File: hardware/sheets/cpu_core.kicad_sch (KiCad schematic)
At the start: 43 parts, among them U1 V20, U10 74HCT32, U11 74HCT125, U12 74HC157, U13 74HCT04, U14 TCM809, U2 74HCT573, U3 74HCT573, U4 74HCT573, U5 74HCT245, U6 74HCT138, U7 74HCT00, U8 74HCT74, U9 74HC161

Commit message: Symbols+parts: IS62WV51216, TL16C550CPT, I2C RTC; 3.3V LVC/HC rebinds
New flat mini-xt: symbols (gensym.py), pins verified against
jlc_get_pinout + datasheet (PCF8563 caught a jlc_get_pinout numbering bug):
IS62WV51216 (512Kx16 SRAM, TSOP-44), TL16C550PT (TL16C550C UART, LQFP-48,
NO.PT numbering -- distinct from the old DIP-40 16550 symbol), PCF8563
(I2C RTC, SO-8).

parts.py: bind the three new parts (SRAM in stock at JLC; TL16C550CPT
sourced elsewhere like the V20, 0 JLC stock; PCF8563 + CR2032 holder on
Device:Battery_Cell); rebind the clock dividers to 74LVC74A/74LVC161
(check 7: HC/HCT both fail fmax margin at 3.3V/14.318MHz); add LVC-grade
binds for 5V-tolerant-input octal parts (74LVC573A/244A/574A/125A/245A)
and plain-HC binds for pure-3.3V-domain gates (74HC00/04/32/138) on the
existing HCT-body symbols; add 74LVC2G07 as a value override on the
pin-identical 74LVC2G06 body. Delete the now-dead AS6C4008 DIP-32 socket,
16550 PLCC-44 socket, and DS12C887 DIP-24 socket entries (replaced parts,
no longer sourced).

Sanity build (build.py) still passes: root + 13 sheets, exit 0. The three
deleted entries leave their still-unrewired sheets (cpu_core, com_port,
rtc) temporarily unmapped in check_parts.py until Tasks 4-9 rewire them --
expected transitional state, not a regression.

Co-Authored-By: Claude Fable 5 <noreply@anthropic.com>
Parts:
- RAM1, RAM2: footprint Package_DIP:DIP-32_W15.24mm_Socket -> (none); LCSC Part Num C2874017 -> (none)
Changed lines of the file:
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@@
 			)
 		)
-		(property "Footprint" "Package_DIP:DIP-32_W15.24mm_Socket"
-			(at 302.26 76.2 0)
-			(effects
-				(font
-					(size 1.27 1.27)
-				)
-				(hide yes)
-			)
-		)
-		(property "LCSC Part Num" "C2874017"
+		(property "Footprint" ""
 			(at 302.26 76.2 0)
 			(effects
@@
 			)
 		)
-		(property "Footprint" "Package_DIP:DIP-32_W15.24mm_Socket"
+		(property "Footprint" ""
 			(at 302.26 175.26 0)
 			(effects
-				(font
-					(size 1.27 1.27)
-				)
-				(hide yes)
-			)
-		)
-		(property "LCSC Part Num" "C2874017"
-			(at 302.26 175.26 0)
-			(effects

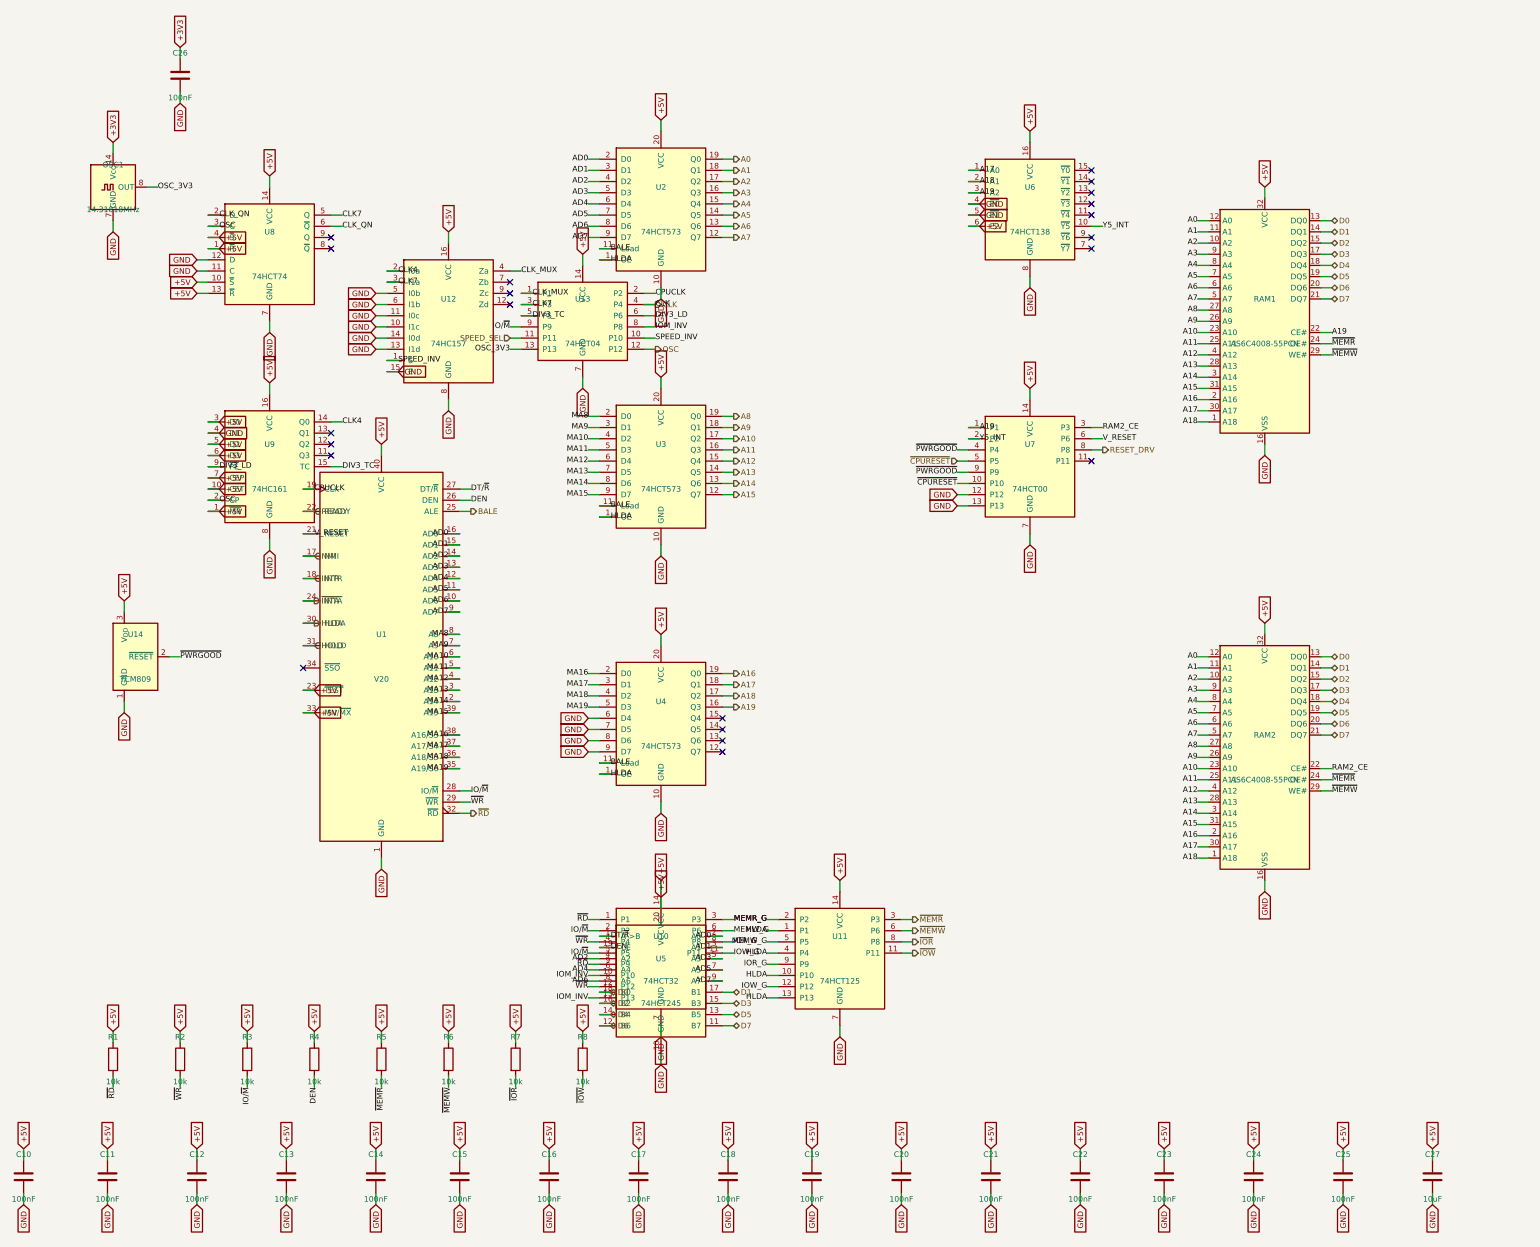
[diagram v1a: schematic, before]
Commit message: cpu_core: LVC573A/245A 3.3V boundary; single 512Kx16 SRAM as 1Mx8
Convert the CPU core to the 3.3V single-board design (spec 2026-07-14): the V20
and its demux latches/transceiver become the board's single 5V<->3.3V boundary.

- Address latches U2-U4 -> 74LVC573A, data xcvr U5 -> 74LVC245A, strobe tri-state
  U11 -> 74LVC125A, all @ +3V3 with 5V-tolerant CPU-side inputs (the boundary).
  U10 74HCT32 stays @ +5V (reads the raw 5V V20 strobes); U13 74HCT04 stays @ +5V
  (V20 CLK needs Vkh=4.0V, Task1 check 1).
- Glue U6 138 / U7 00 -> 74HC values @ +3V3; dividers U8/U9 -> 74LVC74A/74LVC161
  @ +3V3 (Task1 check 7 fmax). Speed mux U12 @ +3V3, select driven directly by
  the 3.3V SPEED_SEL (I0a/I1a un-swapped); U13's freed SPEED gate parked.
- Reset: V20 RESET driven directly from 3.3V logic (Task1 check 1, no buffer);
  TCM809 U14 -> +3V3.
- Memory: drop 2x AS6C4008 + the SRAM#2 select NAND; place 1x IS62WV51216BLL
  512Kx16 as 1Mx8 (byte-lane trick: A0->LB, A0_INV->UB, both IO bytes on D0-D7).
  /CE = NOT(Y5_INT) via a freed U7 NAND-as-inverter (answers 1MB less the
  0xA0000-0xBFFFF video window); A0_INV via the other freed U7 gate.
- Decoupling pool -> +3V3 (drop the removed SRAM's caps); explicit +5V caps for
  the surviving 5V parts.

Decisions logged in hardware/notes/questions-cpu_core.md.

Co-Authored-By: Claude Fable 5 <noreply@anthropic.com>
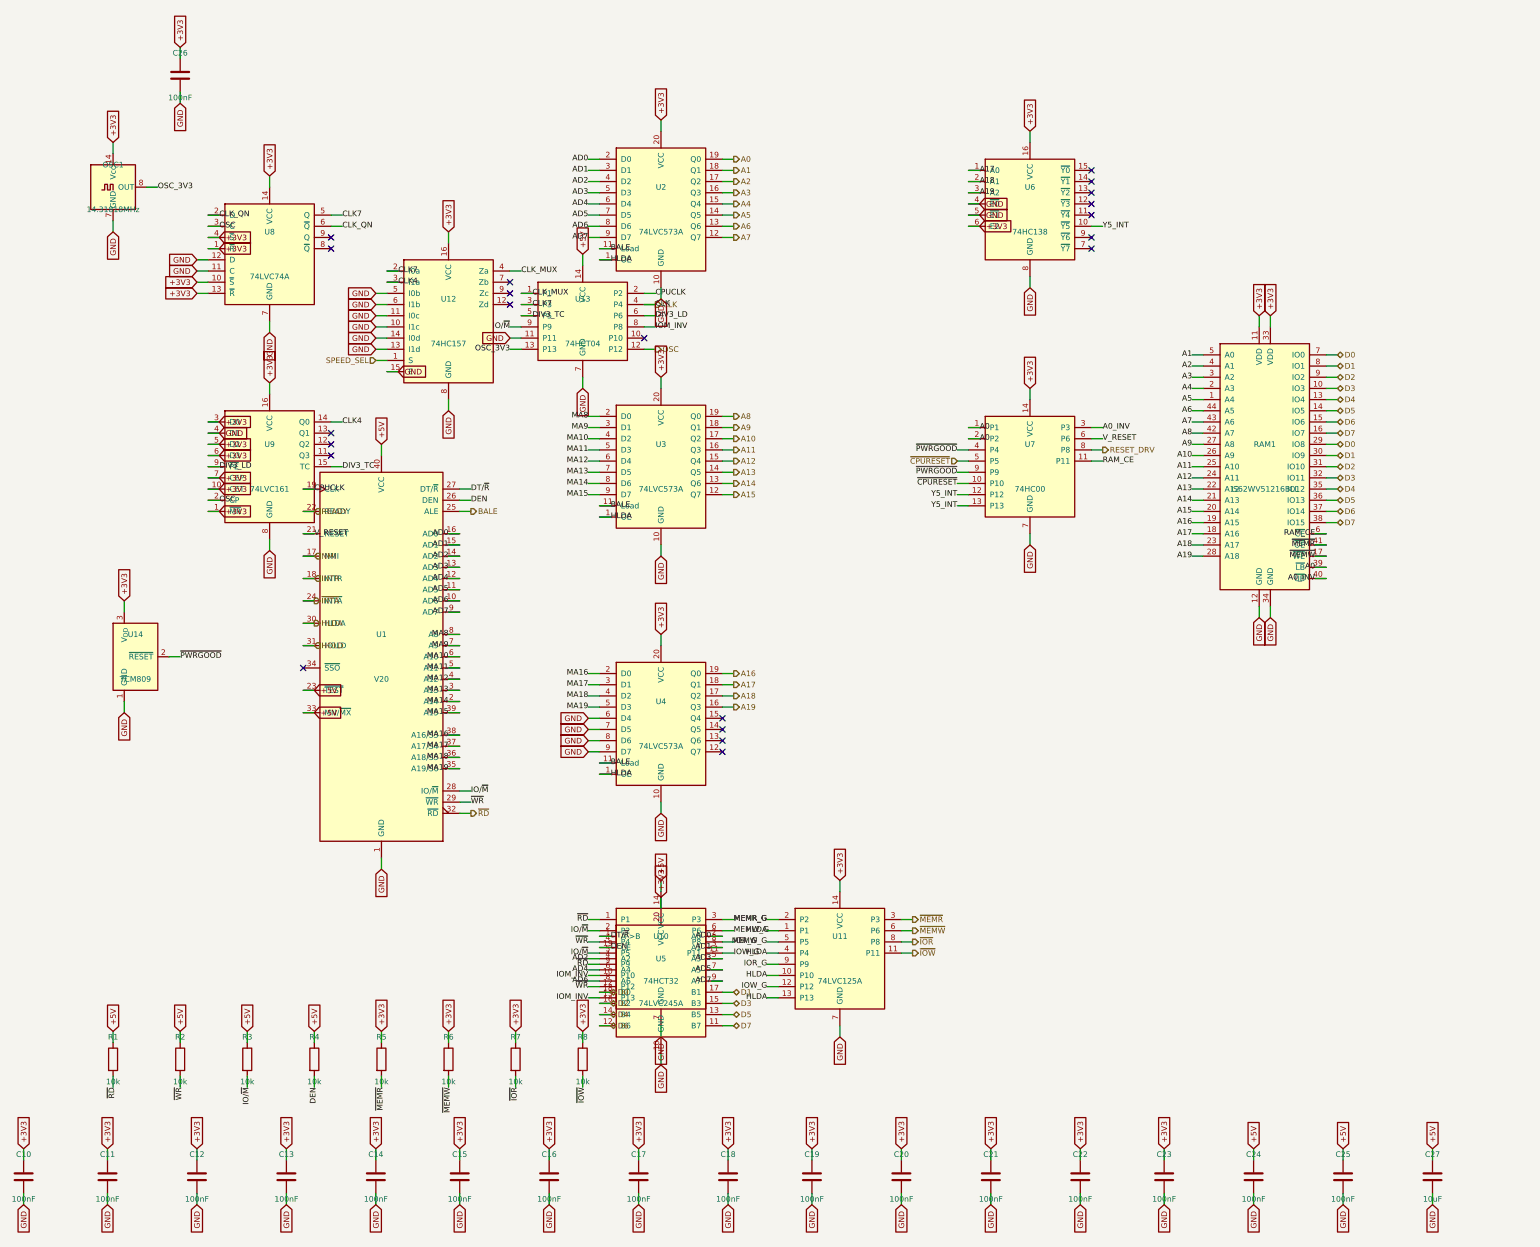
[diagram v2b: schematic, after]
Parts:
- removed RAM1, RAM2: AS6C4008-55PCN, symbol Memory_RAM:AS6C4008-55PCN
- added RAM1: IS62WV51216BLL, Package_SO:TSOP-II-44_10.16x18.41mm_P0.8mm, symbol mini-xt:IS62WV51216
- U11: value 74HCT125 -> 74LVC125A; LCSC Part Num C5962 -> C6057
- U2, U3, U4: value 74HCT573 -> 74LVC573A; footprint Package_SO:SOIC-20W_7.5x12.8mm_P1.27mm -> Package_SO:TSSOP-20_4.4x6.5mm_P0.65mm; LCSC Part Num C5209384 -> C6096
- U5: value 74HCT245 -> 74LVC245A; footprint Package_SO:SOIC-20W_7.5x12.8mm_P1.27mm -> Package_SO:TSSOP-20_4.4x6.5mm_P0.65mm; LCSC Part Num C5979 -> C6082
- U6: value 74HCT138 -> 74HC138; LCSC Part Num C5965 -> C5602
- U7: value 74HCT00 -> 74HC00; LCSC Part Num C282337 -> C699445
- U8: value 74HCT74 -> 74LVC74A; footprint Package_SO:SOIC-14_3.9x8.7mm_P1.27mm -> Package_SO:TSSOP-14_4.4x5mm_P0.65mm; LCSC Part Num C686657 -> C6100
- U9: value 74HC161 -> 74LVC161; footprint Package_SO:SOIC-16_3.9x9.9mm_P1.27mm -> Package_SO:TSSOP-16_4.4x5mm_P0.65mm; LCSC Part Num C5610 -> C548136
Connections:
- net +3V3: now also C10.1, C11.1, C12.1, C13.1, C14.1, C15.1, C16.1, C17.1, C18.1, C19.1, C20.1, C21.1, C22.1, C23.1, R5.1, R6.1, R7.1, R8.1, U11.14 (VCC), U12.16 (VCC), U14.3 (V_{DD}), U2.20 (VCC), U3.20 (VCC), U4.20 (VCC), U5.20 (VCC), U6.16 (VCC), U6.6 (E2), U7.14 (VCC), U8.1 (~{R}), U8.10 (~{S}), U8.13 (~{R}), U8.14 (VCC), U8.4 (~{S}), U9.1 (~{MR}), U9.10 (CET), U9.16 (VCC), U9.3 (D0), U9.5 (D2), U9.6 (D3), U9.7 (CEP), RAM1.11 (VDD), RAM1.33 (VDD)
- net +5V: no longer C10.1, C11.1, C12.1, C13.1, C14.1, C15.1, C16.1, C17.1, C18.1, C19.1, C20.1, C21.1, C22.1, C23.1, R5.1, R6.1, R7.1, R8.1, U11.14 (VCC), U12.16 (VCC), U14.3 (V_{DD}), U2.20 (VCC), U3.20 (VCC), U4.20 (VCC), U5.20 (VCC), U6.16 (VCC), U6.6 (E2), U7.14 (VCC), U8.1 (~{R}), U8.10 (~{S}), U8.13 (~{R}), U8.14 (VCC), U8.4 (~{S}), U9.1 (~{MR}), U9.10 (CET), U9.16 (VCC), U9.3 (D0), U9.5 (D2), U9.6 (D3), U9.7 (CEP)
- net A0: now also U7.1 (P1), U7.2 (P2), RAM1.39 (~{LB})
- net A1: now also RAM1.5 (A0)
- net A10: now also RAM1.26 (A9)
- net A11: now also RAM1.25 (A10)
- net A12: now also RAM1.24 (A11)
- net A13: now also RAM1.22 (A12)
- net A14: now also RAM1.21 (A13)
- net A15: now also RAM1.20 (A14)
- net A16: now also RAM1.19 (A15)
- net A17: now also RAM1.18 (A16)
- net A18: now also RAM1.23 (A17)
- net A19: now also RAM1.28 (A18); no longer U7.1 (P1)
- net A2: now also RAM1.4 (A1)
- net A3: now also RAM1.3 (A2)
- net A4: now also RAM1.2 (A3)
- net A5: now also RAM1.1 (A4)
- net A6: now also RAM1.44 (A5)
- net A7: now also RAM1.43 (A6)
- net A8: now also RAM1.42 (A7)
- net A9: now also RAM1.27 (A8)
- net CLK4: now also U12.3 (I1a); no longer U12.2 (I0a)
- net CLK7: now also U12.2 (I0a); no longer U12.3 (I1a)
- net D0: now also RAM1.29 (IO8), RAM1.7 (IO0)
- net D1: now also RAM1.30 (IO9), RAM1.8 (IO1)
- net D2: now also RAM1.31 (IO10), RAM1.9 (IO2)
- net D3: now also RAM1.10 (IO3), RAM1.32 (IO11)
- net D4: now also RAM1.13 (IO4), RAM1.35 (IO12)
- net D5: now also RAM1.14 (IO5), RAM1.36 (IO13)
- net D6: now also RAM1.15 (IO6), RAM1.37 (IO14)
- net D7: now also RAM1.16 (IO7), RAM1.38 (IO15)
- net GND: now also U13.11 (P11), RAM1.12 (GND), RAM1.34 (GND); no longer U7.12 (P12), U7.13 (P13)
- net SPEED_SEL: now also U12.1 (S); no longer U13.11 (P11)
- net Y5_INT: now also U7.12 (P12), U7.13 (P13); no longer U7.2 (P2)
- net ~{MEMR}: now also RAM1.41 (~{OE})
- net ~{MEMW}: now also RAM1.17 (~{WE})
- net RAM_CE: now reaches U7.11 (P11)
- net RAM_CE: now also RAM1.6 (~{CE})
- net RAM2_CE renamed A0_INV
- net A0_INV: now also RAM1.40 (~{UB})
- net SPEED_INV: no longer names the net of U13.10 (P10)
- net SPEED_INV: no longer U12.1 (S)
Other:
- title: CPU / Memory / Clock / Reset core (5V) -> CPU / Memory / Clock / Reset core (5V<->3.3V boundary)

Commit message: cpu_core: re-buffer BALE/CLK/OSC at 3.3V (review fix)
Review of f6d0d34 found three ISA bus nets driven at 5V (unsafe: they reach
the non-5V-tolerant sidecar RP2040). Added U15 74LVC125A @ +3V3 to re-buffer
BALE (from raw V20 ALE), CLK (from CLK7), and OSC (from OSC_3V3); dividers now
clock off OSC_3V3 directly. U13 74HCT04 keeps only its private CPUCLK gate.

Co-Authored-By: Claude Fable 5 <noreply@anthropic.com>
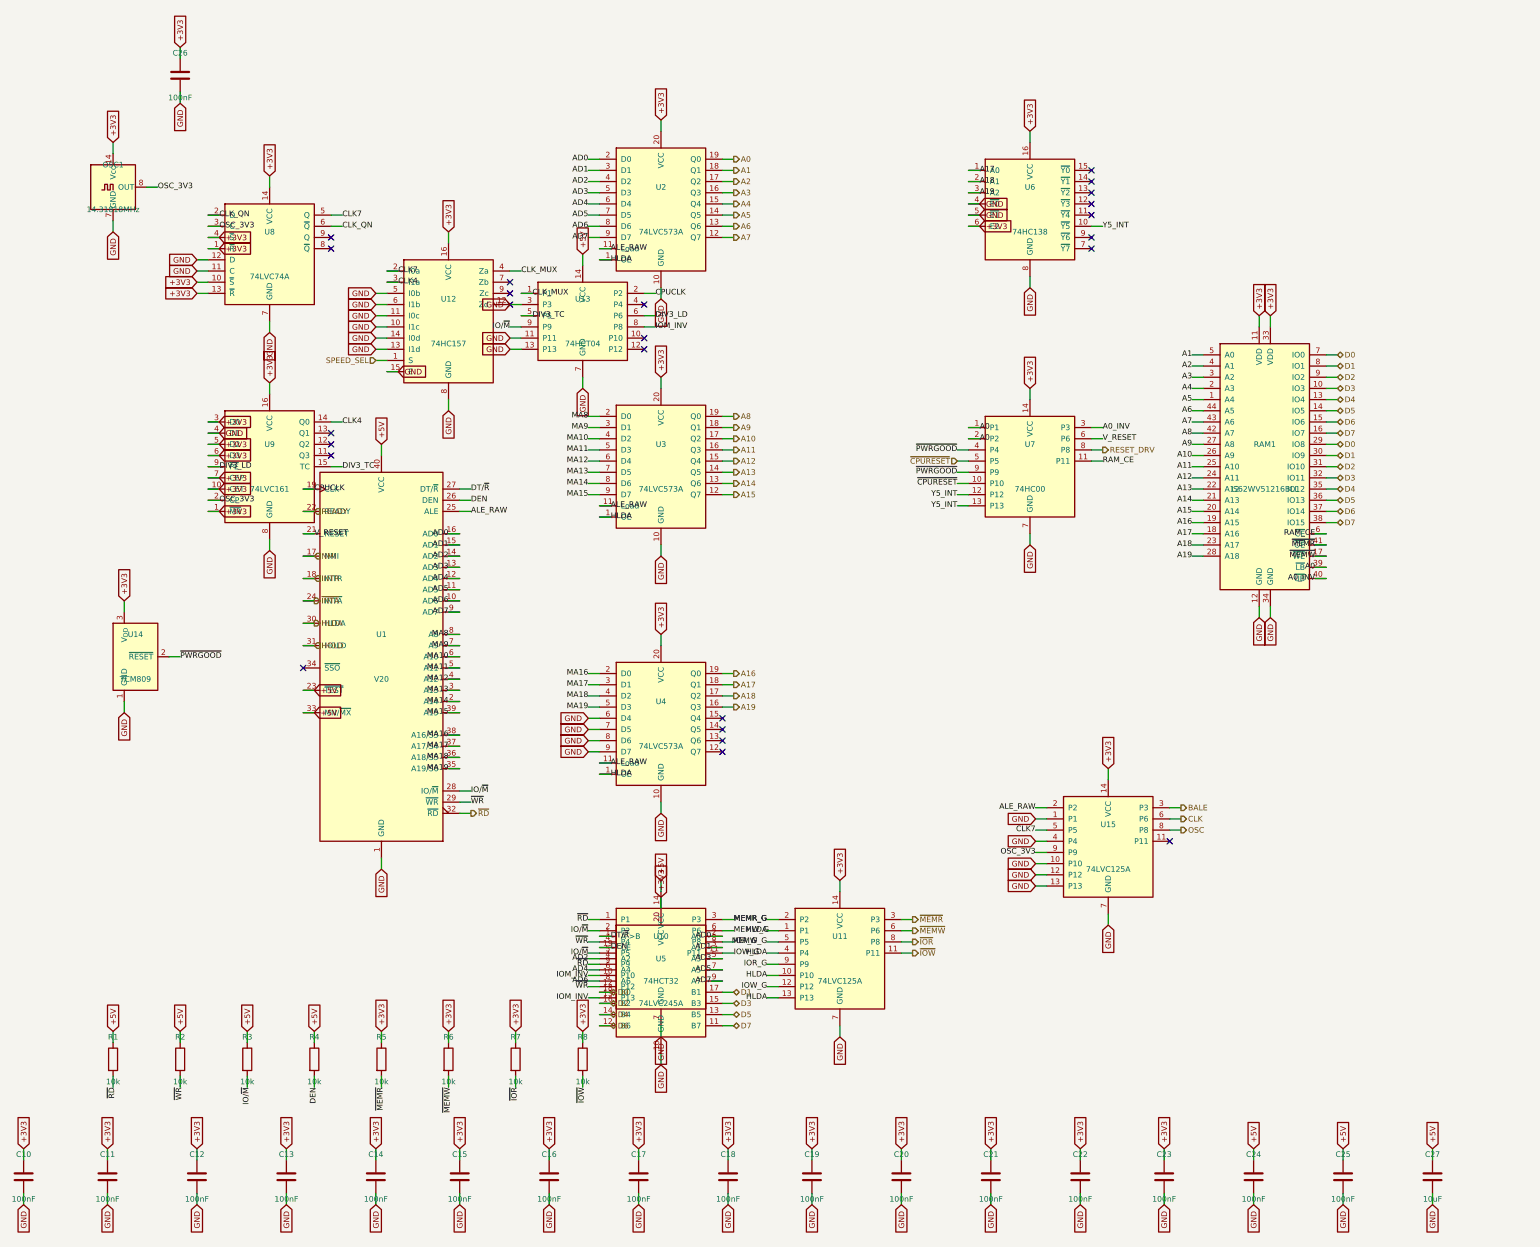
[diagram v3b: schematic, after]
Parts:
- removed U14: TCM809, Package_TO_SOT_SMD:SOT-23, symbol Power_Supervisor:TCM809
- added R2: 10k, Resistor_SMD:R_0603_1608Metric, symbol Device:R
- added U15: 74LVC125A, Package_SO:SOIC-14_3.9x8.7mm_P1.27mm, symbol mini-xt:74HCT125
- U14: renamed from R2; value 10k -> TCM809; footprint Resistor_SMD:R_0603_1608Metric -> Package_TO_SOT_SMD:SOT-23; symbol Device:R -> Power_Supervisor:TCM809; LCSC Part Num C25804 -> C511285
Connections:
- net +3V3: now also U14.3 (V_{DD}), U15.14 (VCC)
- net +5V: now also R2.1; no longer U14.1
- net BALE: now also U15.3 (P3); no longer U1.25 (ALE), U2.11 (Load), U3.11 (Load), U4.11 (Load)
- net CLK: now also U15.6 (P6); no longer U13.4 (P4)
- net CLK7: now also U15.5 (P5); no longer U13.3 (P3)
- net GND: now also U12.12 (Zd), U13.13 (P13), U13.3 (P3), U14.1 (GND), U15.1 (P1), U15.10 (P10), U15.12 (P12), U15.13 (P13), U15.4 (P4), U15.7 (GND)
- net OSC: now also U15.8 (P8); no longer U13.12 (P12), U8.3 (C), U9.2 (CP)
- net OSC_3V3: now also U8.3 (C), U9.2 (CP), U15.9 (P9); no longer U13.13 (P13)
- net ~{PWRGOOD}: now also U14.2 (~{RESET})
- net ~{WR}: now also R2.2; no longer U14.2
- new net ALE_RAW: U1.25 (ALE), U15.2 (P2), U2.11 (Load), U3.11 (Load), U4.11 (Load)
- no-connect marks 21 -> 24

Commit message: cpu_core: 3.3V-threshold reset supervisor; sweep stale DS12C887/AS6C4008 doc refs
Co-Authored-By: Claude Fable 5 <noreply@anthropic.com>
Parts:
- U14: LCSC Part Num C511285 -> C47195
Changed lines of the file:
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@@
 			)
 		)
-		(property "LCSC Part Num" "C511285"
+		(property "LCSC Part Num" "C47195"
 			(at 45.72 152.4 0)
 			(effects
